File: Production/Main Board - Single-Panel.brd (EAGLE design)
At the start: 186.9 x 99.3 mm, 180 parts, among them J1 MICROMOD-2222-C, J10 MICRO-SD-PUSH-PUSH-EXT-PIN, J11 MICROMOD-2222-C, J12 CORTEX_JTAG_DEBUG_MINIMUM_PTH, J15 MICROMOD_CARRIER, J16 MICRO-SD-PUSH-PUSH-EXT-PIN, J2 Vertical Qwiic Connector, J4 QWIIC_RIGHT_ANGLE, J5 CORTEX_JTAG_DEBUG_MINIMUM_PTH, J6 MICROMOD_CARRIER, J7 Vertical Qwiic Connector, J9 QWIIC_RIGHT_ANGLE, Q1 3.1A/30V/105mΩ, Q2 3.1A/30V/105mΩ, U1 AP7361C-33, U2 MCP73831, U3 MCP73831, U5 AP7361C-33

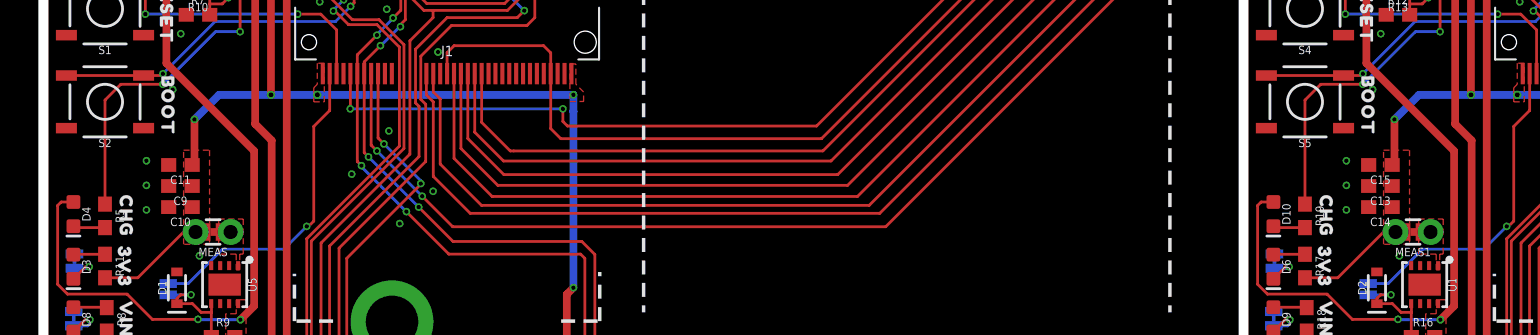
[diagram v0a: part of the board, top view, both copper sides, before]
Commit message: Adds new panel
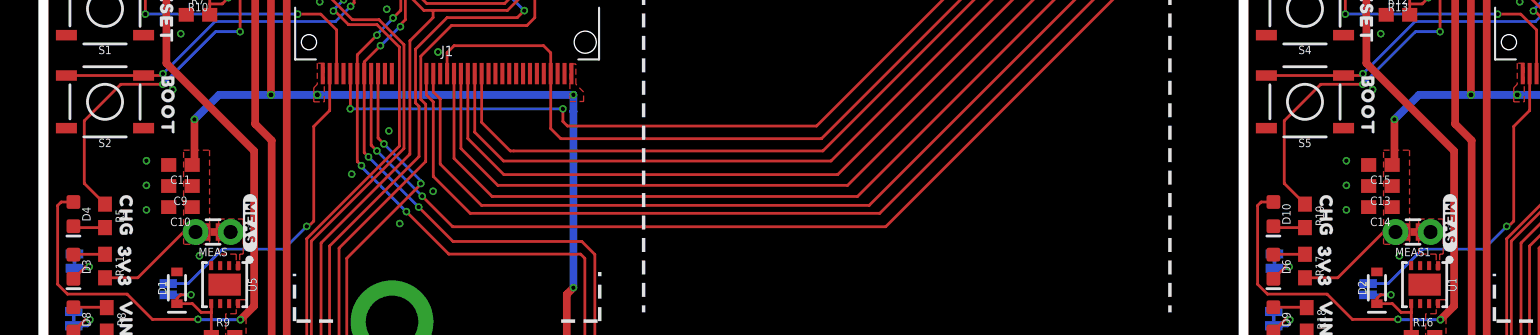
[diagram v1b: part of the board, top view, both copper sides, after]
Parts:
- added U$45: (no value), SparkFun-Aesthetics:SFE_LOGO_FLAME_.2
- added U$46: (no value), top:#MEAS#40313513
- U$23: device top:3V332530 -> top:#MEAS#40313513
- U$24: device top:VIN32529 -> top:3V332530
- U$25: device top:CHG32528 -> top:VIN32529
- U$26: device top:FUNCTION_ZERO517 -> top:CHG32528
- U$27: device top:PROCESSOR522 -> top:FUNCTION_ZERO517
- U$28: device top:#3V3_LED#17 -> top:PROCESSOR522
- U$29: device top:#VIN_LED#16 -> top:#3V3_LED#17
- U$30: device top:#PTC#18 -> top:#VIN_LED#16
- U$31: device top:BOOT32541 -> top:#PTC#18
- U$32: device top:RESET32540 -> top:BOOT32541
- U$33: device top:#3V3_EN#18 -> top:RESET32540
- U$34: device SparkFun-MicroMod:MICROMOD_MI_LOGO_1 -> top:#3V3_EN#18
- U$35: device top:0525 -> SparkFun-MicroMod:MICROMOD_MI_LOGO_1
- U$36: device top:MAIN523 -> top:0525
- U$37: device top:BOARD524 -> top:MAIN523
- U$38: device top:100MA6 -> top:BOARD524
- U$39: device top:500MA101 -> top:100MA6
- U$40: device top:MAIN_BOARD5523 -> top:500MA101
- U$41: device SparkFun-MicroMod:MICROMOD_LOGO_1 -> top:MAIN_BOARD5523
- U$42: device SparkFun-Aesthetics:QWIIC_3MM -> SparkFun-MicroMod:MICROMOD_LOGO_1
- U$43: device top:STANDOFF501 -> SparkFun-Aesthetics:QWIIC_3MM
- U$44: device SparkFun-Aesthetics:SFE_LOGO_FLAME_.2 -> top:STANDOFF501
- moved U$23 77.8 mm to (14.7, 34.4)
- moved U$38 69.8 mm to (141.2, 16.8), flipped to the bottom, turned to 0 degrees
- moved U$26 67.6 mm to (92.6, 34.9), turned to 270 degrees
- moved U$42 57.4 mm to (146.7, 23.5), flipped to the bottom
- moved U$41 47.1 mm to (118.7, 61.5), flipped to the top
- moved U$35 44.9 mm to (104.9, 62.0)
- moved U$36 38.7 mm to (149.4, 55.4), flipped to the top
- moved U$27 38.6 mm to (149.5, 71.4)
- moved U$34 32.8 mm to (98.9, 29.7), flipped to the bottom
- moved U$28 32.1 mm to (114.4, 55.2), flipped to the top
- moved U$31 30.1 mm to (95.4, 12.8), flipped to the bottom, turned to 0 degrees
- moved U$33 20.4 mm to (95.5, 49.8), flipped to the top, turned to 270 degrees
- moved U$40 19.6 mm to (100.5, 68.5), turned to 270 degrees
- moved U$30 15.0 mm to (92.3, 27.5)
- moved U$37 11.9 mm to (153.2, 16.9)
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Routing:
- net N$15: track 30.2 -> 31.4 mm
- net N$24: track 30.2 -> 31.4 mm
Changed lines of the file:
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@@
 <attribute name="VALUE" x="7.239" y="18.161" size="0.6096" layer="27" font="vector" ratio="20" rot="R270" align="top-center"/>
 </element>
+<element name="U$23" library="top" package="#MEAS#40313513" value="" x="14.69" y="34.41" smashed="yes" rot="R270"/>
 <element name="J7" library="SparkFun-Connectors" package="JST04_1MM_VERT" value="Vertical Qwiic Connector" x="124.968" y="11.43" smashed="yes">
 <attribute name="NAME" x="124.984" y="15.99633125" size="0.6096" layer="25"/>
@@
 <element name="LOGO5" library="SparkFun-Aesthetics" package="SFE_LOGO_NAME_FLAME_.3" value="SFE_LOGO_NAME_FLAME.3_INCH" x="149.098" y="30.48" smashed="yes" rot="MR0"/>
 <element name="LOGO6" library="SparkFun-Aesthetics" package="OSHW-LOGO-L" value="OSHW-LOGOL" x="168.656" y="8.382" smashed="yes" rot="MR0"/>
-<element name="U$23" library="top" package="3V332530" value="" x="92.456" y="31.242" smashed="yes" rot="R270"/>
-<element name="U$24" library="top" package="VIN32529" value="" x="92.583" y="27.432" smashed="yes" rot="R270"/>
-<element name="U$25" library="top" package="CHG32528" value="" x="92.583" y="34.925" smashed="yes" rot="R270"/>
-<element name="U$26" library="top" package="FUNCTION_ZERO517" value="" x="149.479" y="71.374" smashed="yes"/>
-<element name="U$27" library="top" package="PROCESSOR522" value="" x="114.427" y="55.245" smashed="yes"/>
-<element name="U$28" library="top" package="#3V3_LED#17" value="" x="92.456" y="31.7754" smashed="yes" rot="MR0"/>
-<element name="U$29" library="top" package="#VIN_LED#16" value="" x="92.2528" y="27.4574" smashed="yes" rot="MR0"/>
-<element name="U$30" library="top" package="#PTC#18" value="" x="95.4024" y="12.7762" smashed="yes" rot="MR0"/>
-<element name="U$31" library="top" package="BOOT32541" value="" x="95.6056" y="42.9006" smashed="yes" rot="R270"/>
-<element name="U$32" library="top" package="RESET32540" value="" x="95.504" y="49.784" smashed="yes" rot="R270"/>
-<element name="U$33" library="top" package="#3V3_EN#18" value="" x="98.9076" y="29.6926" smashed="yes" rot="MR0"/>
+<element name="U$24" library="top" package="3V332530" value="" x="92.456" y="31.242" smashed="yes" rot="R270"/>
+<element name="U$25" library="top" package="VIN32529" value="" x="92.583" y="27.432" smashed="yes" rot="R270"/>
+<element name="U$26" library="top" package="CHG32528" value="" x="92.583" y="34.925" smashed="yes" rot="R270"/>
+<element name="U$27" library="top" package="FUNCTION_ZERO517" value="" x="149.479" y="71.374" smashed="yes"/>
+<element name="U$28" library="top" package="PROCESSOR522" value="" x="114.427" y="55.245" smashed="yes"/>
+<element name="U$29" library="top" package="#3V3_LED#17" value="" x="92.456" y="31.7754" smashed="yes" rot="MR0"/>
+<element name="U$30" library="top" package="#VIN_LED#16" value="" x="92.2528" y="27.4574" smashed="yes" rot="MR0"/>
+<element name="U$31" library="top" package="#PTC#18" value="" x="95.4024" y="12.7762" smashed="yes" rot="MR0"/>
+<element name="U$32" library="top" package="BOOT32541" value="" x="95.6056" y="42.9006" smashed="yes" rot="R270"/>
+<element name="U$33" library="top" package="RESET32540" value="" x="95.504" y="49.784" smashed="yes" rot="R270"/>
+<element name="U$34" library="top" package="#3V3_EN#18" value="" x="98.9076" y="29.6926" smashed="yes" rot="MR0"/>
 <element name="H12" library="SparkFun-Hardware" package="STAND-OFF-TIGHT" value="STAND-OFFTIGHT" x="89.408" y="22.86" smashed="yes">
 <attribute name="NAME" x="89.408" y="24.511" size="0.6096" layer="25" font="vector" ratio="20" align="bottom-center"/>
 <attribute name="VALUE" x="89.408" y="21.209" size="0.6096" layer="27" font="vector" ratio="20" align="top-center"/>
 </element>
-<element name="U$34" library="SparkFun-MicroMod" package="MICROMOD_MI_LOGO_1" value="" x="104.902" y="61.976" smashed="yes"/>
-<element name="U$35" library="top" package="0525" value="" x="149.352" y="55.372" smashed="yes"/>
-<element name="U$36" library="top" package="MAIN523" value="" x="153.162" y="16.891" smashed="yes" rot="MR0"/>
-<element name="U$37" library="top" package="BOARD524" value="" x="141.224" y="16.764" smashed="yes" rot="MR0"/>
+<element name="U$35" library="SparkFun-MicroMod" package="MICROMOD_MI_LOGO_1" value="" x="104.902" y="61.976" smashed="yes"/>
+<element name="U$36" library="top" package="0525" value="" x="149.352" y="55.372" smashed="yes"/>
+<element name="U$37" library="top" package="MAIN523" value="" x="153.162" y="16.891" smashed="yes" rot="MR0"/>
+<element name="U$38" library="top" package="BOARD524" value="" x="141.224" y="16.764" smashed="yes" rot="MR0"/>
 <element name="S6" library="SparkFun-Switches" package="DIPSWITCH-02-50MIL" value="DIP-02-SMD-50MIL" x="97.409" y="68.58" smashed="yes" rot="R180">
 <attribute name="NAME" x="99.568" y="68.58" size="0.6096" layer="25" font="vector" ratio="20" rot="R270" align="bottom-center"/>
@@
 <attribute name="VALUE" value="3.1A/30V/105mΩ" x="97.536" y="19.812" size="0.6096" layer="27" font="vector" ratio="20" rot="R180" align="top-center"/>
 </element>
-<element name="U$38" library="top" package="100MA6" value="" x="94.361" y="68.453" smashed="yes" rot="R270"/>
-<element name="U$39" library="top" package="500MA101" value="" x="100.457" y="68.453" smashed="yes" rot="R270"/>
-<element name="U$40" library="top" package="MAIN_BOARD5523" value="" x="118.745" y="61.468" smashed="yes"/>
-<element name="U$41" library="SparkFun-MicroMod" package="MICROMOD_LOGO_1" value="" x="146.685" y="23.495" smashed="yes" rot="MR0"/>
-<element name="U$42" library="SparkFun-Aesthetics" package="QWIIC_3MM" value="" x="89.408" y="20.32" smashed="yes"/>
-<element name="U$43" library="top" package="STANDOFF501" value="" x="90.424" y="19.177" smashed="yes"/>
-<element name="U$44" library="SparkFun-Aesthetics" package="SFE_LOGO_FLAME_.2" value="" x="89.618" y="13.54" smashed="yes"/>
+<element name="U$39" library="top" package="100MA6" value="" x="94.361" y="68.453" smashed="yes" rot="R270"/>
+<element name="U$40" library="top" package="500MA101" value="" x="100.457" y="68.453" smashed="yes" rot="R270"/>
+<element name="U$41" library="top" package="MAIN_BOARD5523" value="" x="118.745" y="61.468" smashed="yes"/>
+<element name="U$42" library="SparkFun-MicroMod" package="MICROMOD_LOGO_1" value="" x="146.685" y="23.495" smashed="yes" rot="MR0"/>
+<element name="U$43" library="SparkFun-Aesthetics" package="QWIIC_3MM" value="" x="89.408" y="20.32" smashed="yes"/>
+<element name="U$44" library="top" package="STANDOFF501" value="" x="90.424" y="19.177" smashed="yes"/>
+<element name="U$45" library="SparkFun-Aesthetics" package="SFE_LOGO_FLAME_.2" value="" x="89.618" y="13.54" smashed="yes"/>
 <element name="R22" library="SparkFun-Resistors" package="0603" value="10k" x="94.869" y="18.161" smashed="yes" rot="R270">
 <attribute name="NAME" x="95.631" y="18.161" size="0.6096" layer="25" font="vector" ratio="20" rot="R270" align="bottom-center"/>
@@
 <attribute name="VALUE" x="94.107" y="18.161" size="0.6096" layer="27" font="vector" ratio="20" rot="R270" align="top-center"/>
 </element>
+<element name="U$46" library="top" package="#MEAS#40313513" value="" x="101.558" y="34.41" smashed="yes" rot="R270"/>
 <element name="E$1" library="SparkFun-Aesthetics" package="FIDUCIAL-1X2" value="" x="6.858" y="79.5655" smashed="yes"/>
 <element name="E$2" library="SparkFun-Aesthetics" package="FIDUCIAL-1X2" value="" x="6.858" y="79.5655" smashed="yes" rot="MR0"/>
@@
 <contactref element="R5" pad="1"/>
 <contactref element="U2" pad="1"/>
-<wire x1="4.191" y1="35.775" x2="4.191" y2="43.307" width="0.2032" layer="1"/>
+<wire x1="2.691" y1="41.807" x2="2.691" y2="37.275" width="0.2032" layer="1"/>
+<wire x1="4.191" y1="35.775" x2="2.691" y2="37.275" width="0.2032" layer="1"/>
 <wire x1="5.334" y1="44.45" x2="8.382" y2="44.45" width="0.2032" layer="1"/>
-<wire x1="4.191" y1="43.307" x2="5.334" y2="44.45" width="0.2032" layer="1"/>
+<wire x1="2.691" y1="41.807" x2="5.334" y2="44.45" width="0.2032" layer="1"/>
 <via x="8.382" y="44.45" extent="1-16" drill="0.3048"/>
 <wire x1="8.382" y1="44.45" x2="12.192" y2="48.26" width="0.2032" layer="16"/>
@@
 <contactref element="R19" pad="1"/>
 <contactref element="U3" pad="1"/>
-<wire x1="91.059" y1="35.775" x2="91.059" y2="43.307" width="0.2032" layer="1"/>
+<wire x1="89.559" y1="41.807" x2="89.559" y2="37.275" width="0.2032" layer="1"/>
+<wire x1="91.059" y1="35.775" x2="89.559" y2="37.275" width="0.2032" layer="1"/>
 <wire x1="92.202" y1="44.45" x2="95.25" y2="44.45" width="0.2032" layer="1"/>
-<wire x1="91.059" y1="43.307" x2="92.202" y2="44.45" width="0.2032" layer="1"/>
+<wire x1="89.559" y1="41.807" x2="92.202" y2="44.45" width="0.2032" layer="1"/>
 <via x="95.25" y="44.45" extent="1-16" drill="0.3048"/>
 <wire x1="95.25" y1="44.45" x2="99.06" y2="48.26" width="0.2032" layer="16"/>
